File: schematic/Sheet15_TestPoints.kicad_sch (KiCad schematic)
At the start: 18 parts

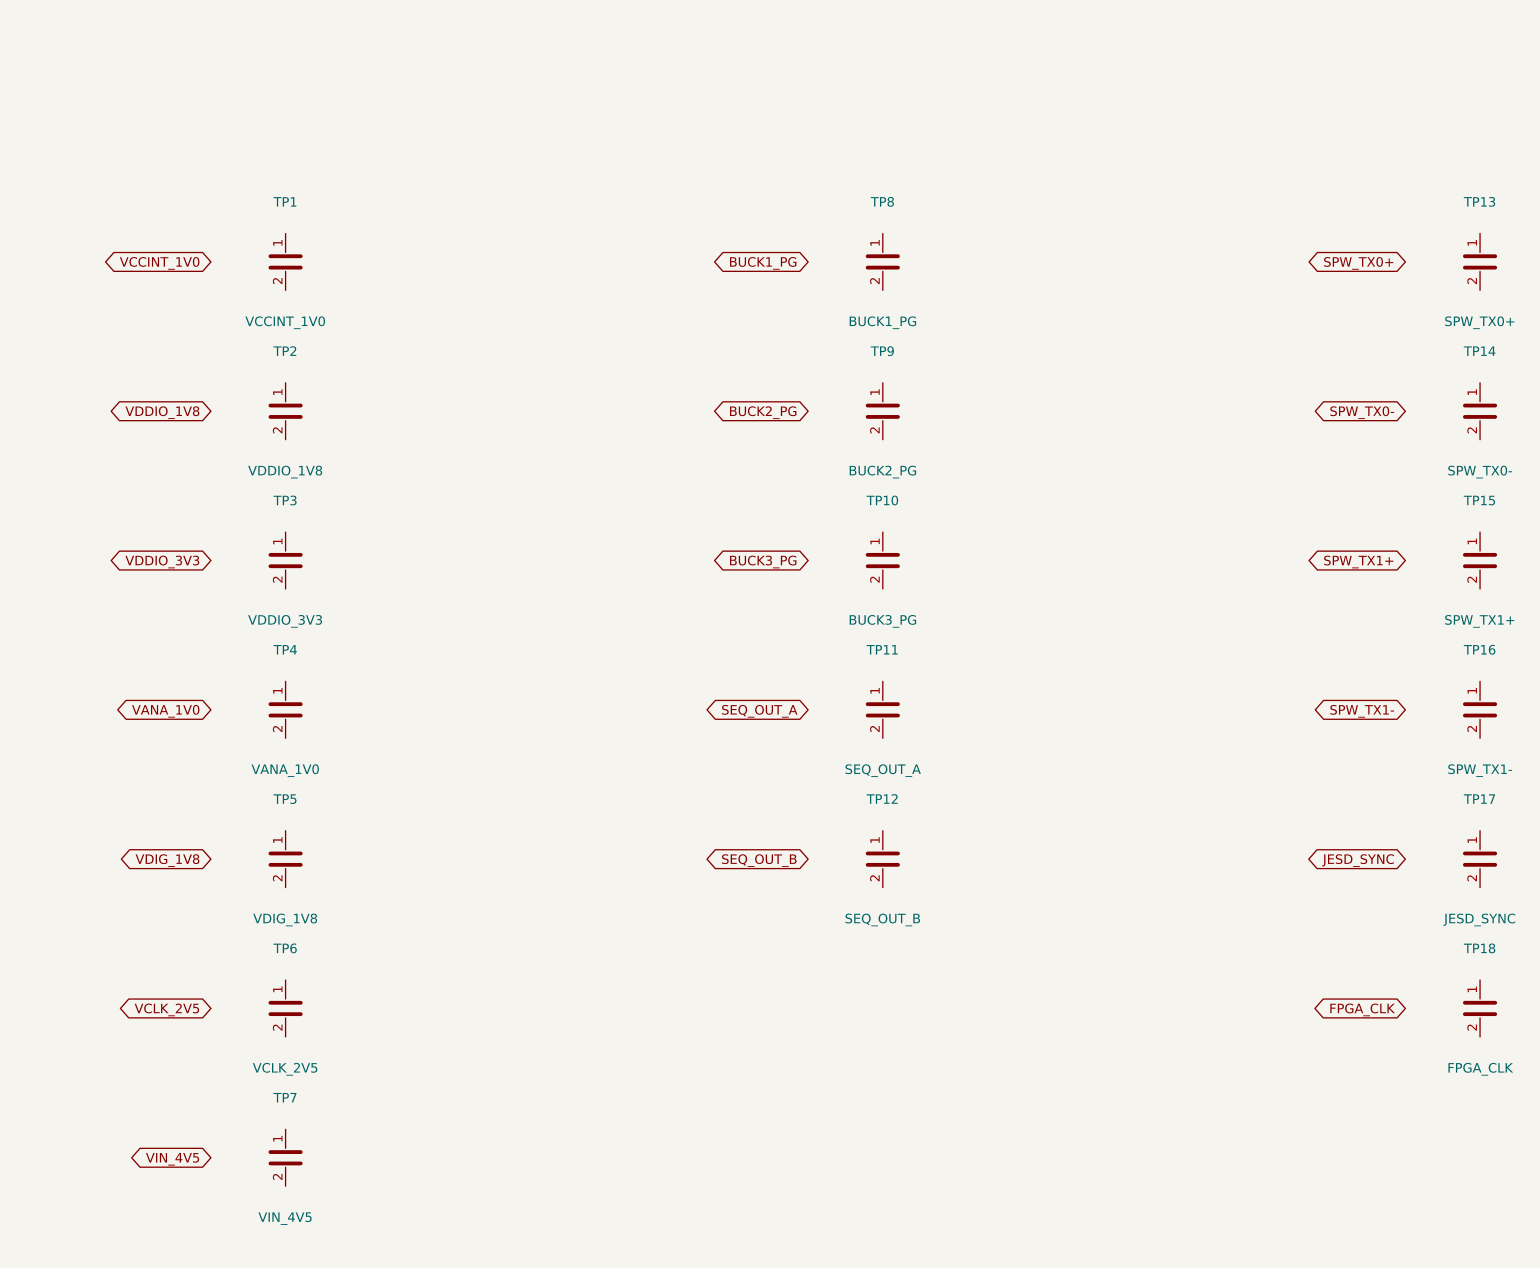
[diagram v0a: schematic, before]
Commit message: feat: real IC schematics with proper pin connections
- ADC12DJ5200-SP: 20 left pins (power, SPI, analog) + 21 right pins (JESD204C)
- XQRVC1902-SP: 19 left pins (power) + 30 right pins (JTAG, SPW, JESD, config)
- TPS7H5002-SP: 9 left + 7 right pins (buck converter 1.0V core)
- ISL70003ASEH: 7 left + 5 right (buck 1.8V/3.3V)
- LMX2615-SP: 8+8 pins (PLL synthesizer)
- LMK04832-SP: 12+12 pins (clock distributor)
- TPS7H1111-SP / TPS7H1121-SP: 3+3 pins (LDOs)
- TPS7H3014-SP: 4+4 pins (sequencer)
- INA214-SP: 3+2 pins (current sense)
- CVHD-950: 3+2 pins (VCXO)

Sheets:
- 02: SMA→50Ω match→anti-alias→ADC analog input
- 03: ADC decoupling, JESD outputs, SPI control
- 04: FPGA 14x decoupling caps, JTAG, SPW, JESD
- 05: Crystek→LMX2615→LMK04832→ADC+FPGA clock tree
- 06-09: Power input, TPS7H5002 buck 1.0V, ISL70003A buck 1.8V/3.3V
- 10-12: LDO 1.0V analog, 1.8V digital, 2.5V clock
- 13: 2x TPS7H3014 power sequencer
- 14: JTAG/SPW/UART connectors
- 15-17: Test points, decoupling, power tree diagram

All 17 sheets export via kicad-cli, merged PDF: 1.1MB
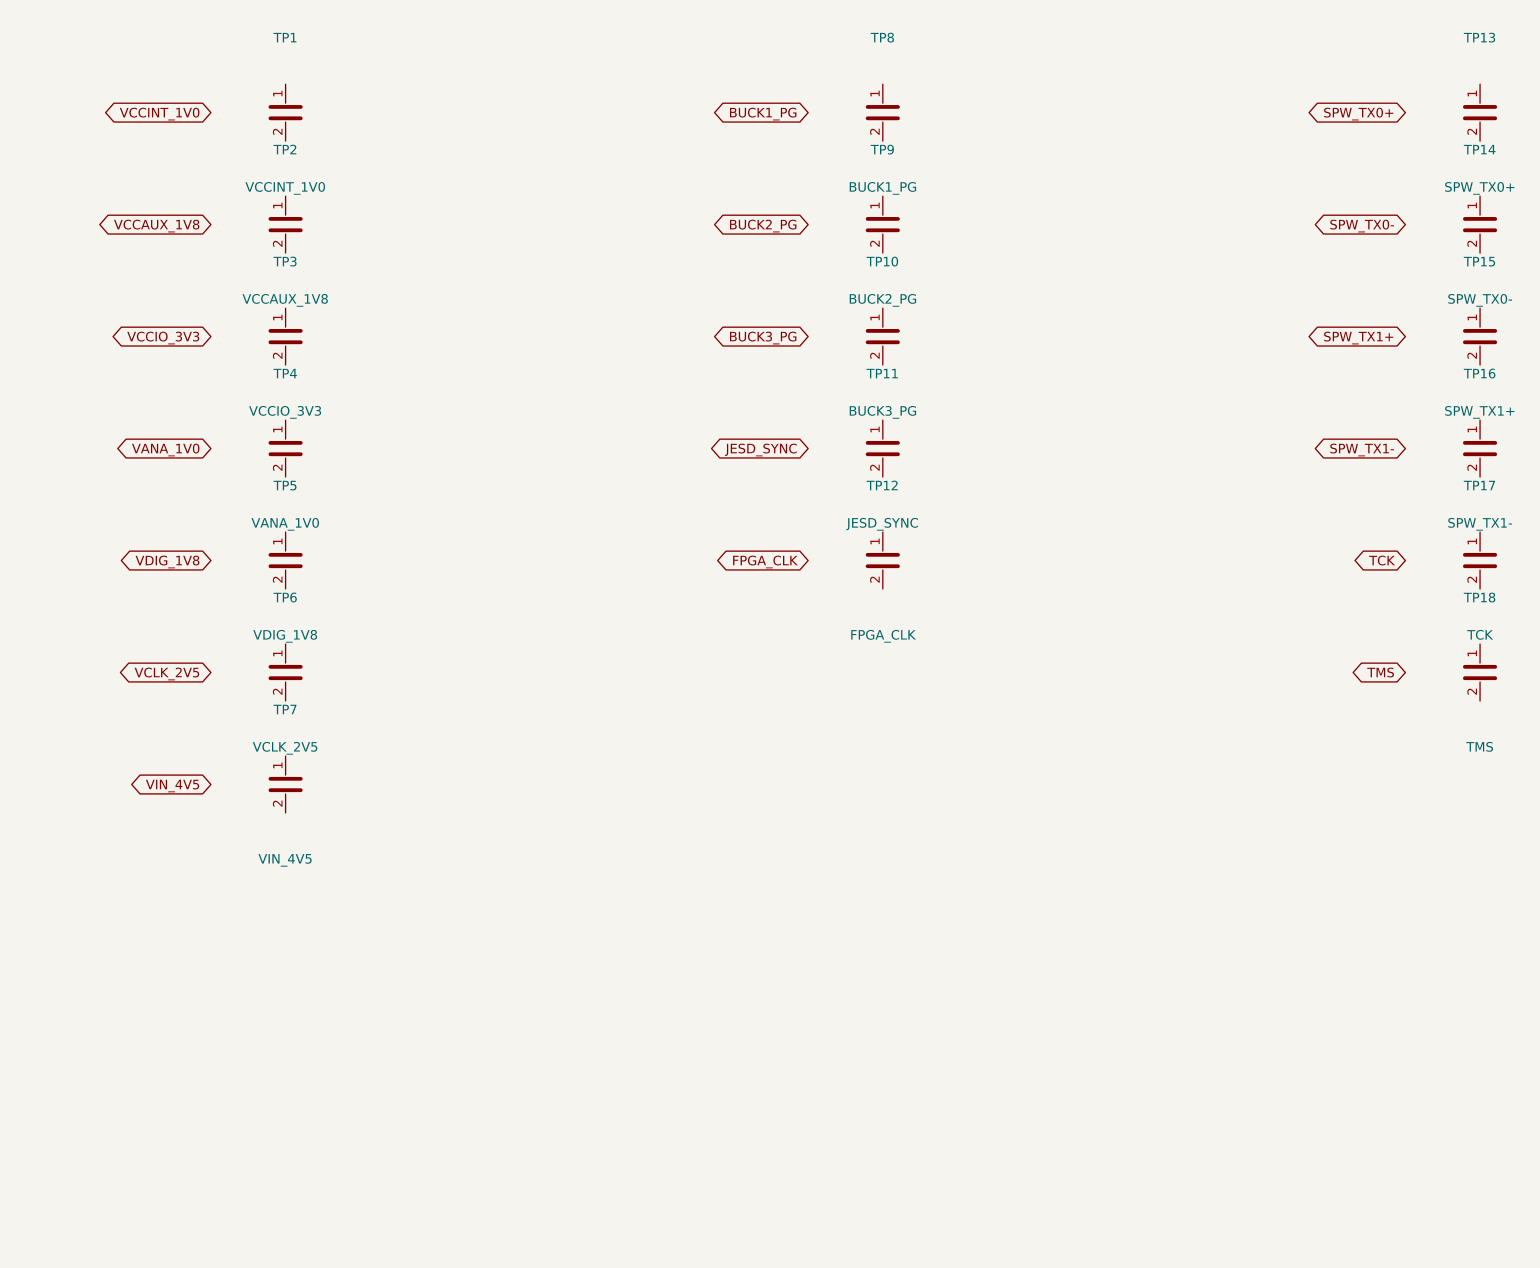
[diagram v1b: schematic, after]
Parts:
- TP1, TP10, TP13, TP14, TP15, TP16, TP4, TP5, TP6, TP7, TP8, TP9: footprint TestPoint:TestPoint_Pad_1.5x1.5mm -> TestPoint
- TP11: value SEQ_OUT_A -> JESD_SYNC; footprint TestPoint:TestPoint_Pad_1.5x1.5mm -> TestPoint
- TP12: value SEQ_OUT_B -> FPGA_CLK; footprint TestPoint:TestPoint_Pad_1.5x1.5mm -> TestPoint
- TP17: value JESD_SYNC -> TCK; footprint TestPoint:TestPoint_Pad_1.5x1.5mm -> TestPoint
- TP18: value FPGA_CLK -> TMS; footprint TestPoint:TestPoint_Pad_1.5x1.5mm -> TestPoint
- TP2: value VDDIO_1V8 -> VCCAUX_1V8; footprint TestPoint:TestPoint_Pad_1.5x1.5mm -> TestPoint
- TP3: value VDDIO_3V3 -> VCCIO_3V3; footprint TestPoint:TestPoint_Pad_1.5x1.5mm -> TestPoint

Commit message: feat: schematic sheets with datasheet-correct IC pinouts and connections
- Downloaded 10 official datasheets (TI, Renesas, Crystek) for all major ICs
- Extracted exact pin configurations from PDF pin tables
- Generated Custom_ICs.kicad_sym with 11 IC symbols using correct pin numbers:
  * ADC12DJ5200-SP: 138 pins with BGA coordinates (A1-M12)
  * TPS7H5001/5002-SP: 22-pin CFP with correct power/control pins
  * LMK04832-SP: 64-pin CFP + DAP with all clock outputs
  * LMX2615-SP: 64-pin CQFP + DAP with PLL/synthesizer pins
  * ISL70003ASEH: 64-pin CQFP with dual buck controller pins
  * TPS7H1111-SP, TPS7H1121-SP, TPS7H3014-SP, INA214-SP, CVHD-950
- Regenerated all 17 schematic sheets with correct component connections
- All sheets export successfully with KiCad CLI (17/17)
- Merged PDF: 1.3MB, 17 pages
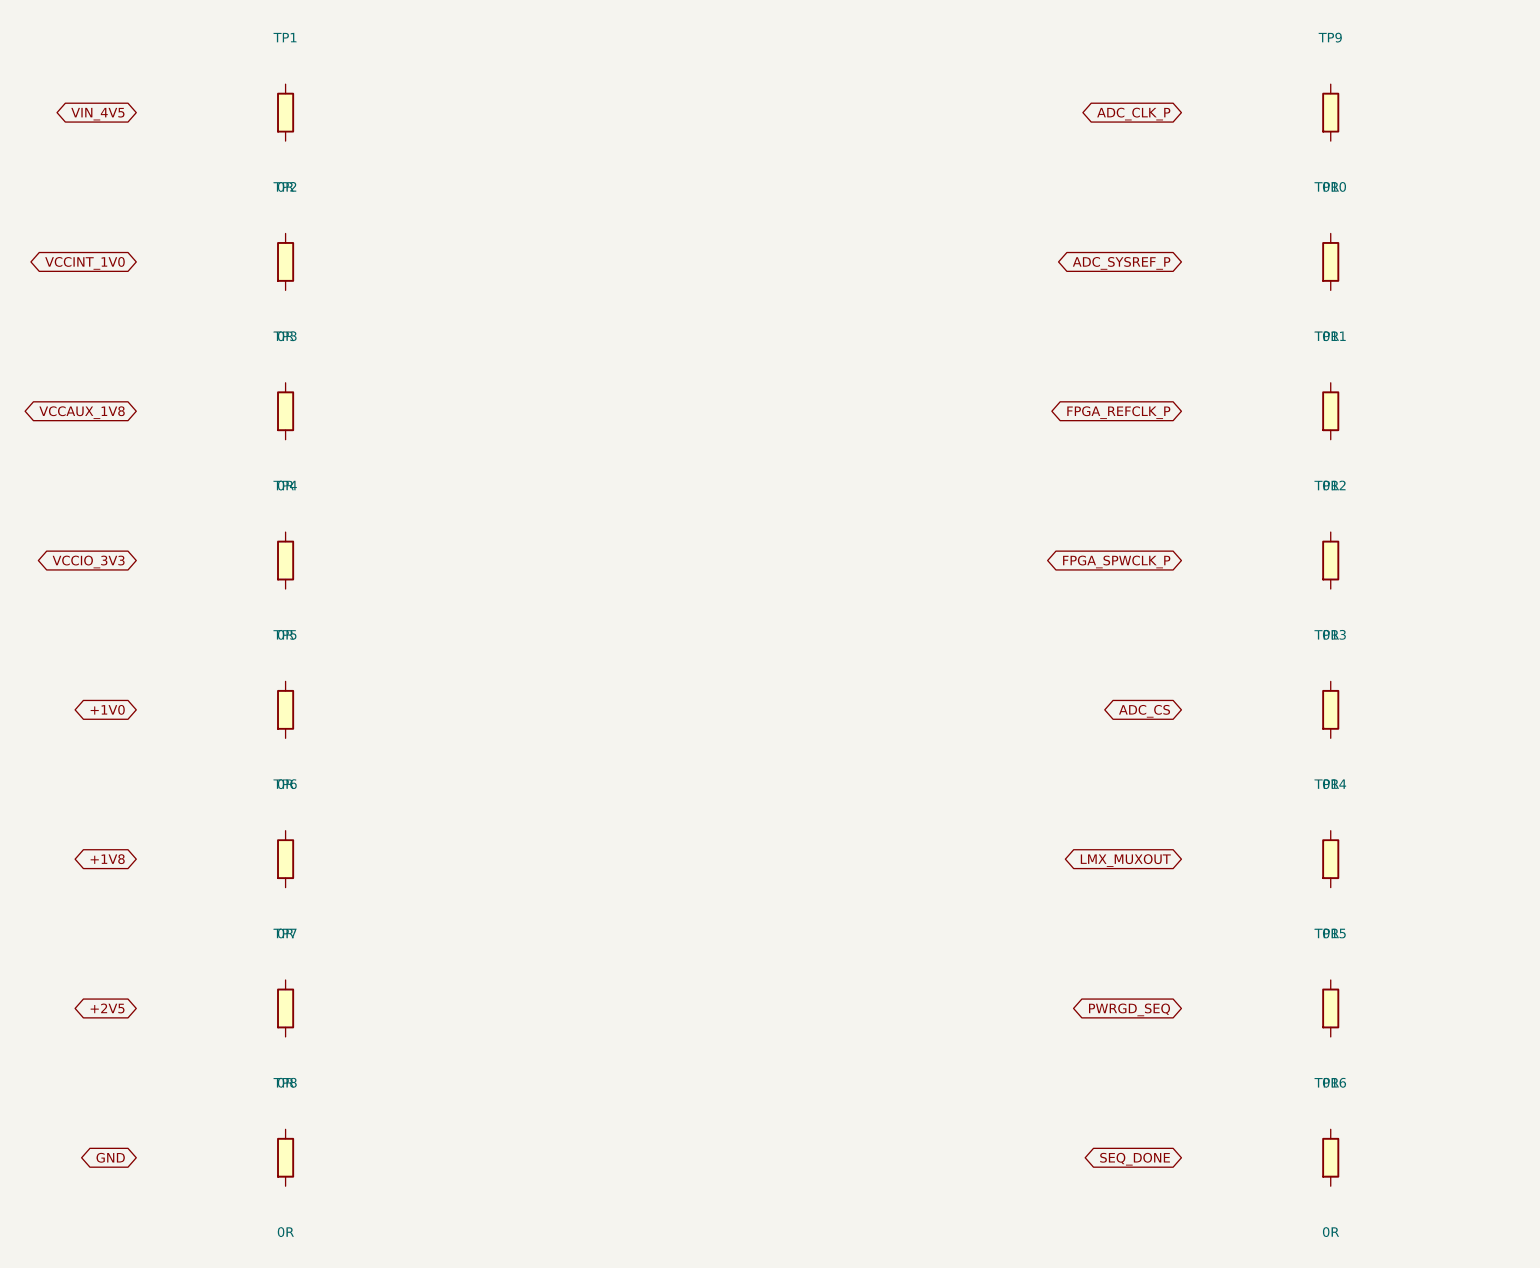
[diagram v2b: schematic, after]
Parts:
- removed TP1: VCCINT_1V0, TestPoint, symbol Device:C
- removed TP10: BUCK3_PG, TestPoint, symbol Device:C
- removed TP11: JESD_SYNC, TestPoint, symbol Device:C
- removed TP12: FPGA_CLK, TestPoint, symbol Device:C
- removed TP13: SPW_TX0+, TestPoint, symbol Device:C
- removed TP14: SPW_TX0-, TestPoint, symbol Device:C
- removed TP15: SPW_TX1+, TestPoint, symbol Device:C
- removed TP16: SPW_TX1-, TestPoint, symbol Device:C
- removed TP17: TCK, TestPoint, symbol Device:C
- removed TP18: TMS, TestPoint, symbol Device:C
- removed TP2: VCCAUX_1V8, TestPoint, symbol Device:C
- removed TP3: VCCIO_3V3, TestPoint, symbol Device:C
- removed TP4: VANA_1V0, TestPoint, symbol Device:C
- removed TP5: VDIG_1V8, TestPoint, symbol Device:C
- removed TP6: VCLK_2V5, TestPoint, symbol Device:C
- removed TP7: VIN_4V5, TestPoint, symbol Device:C
- removed TP8: BUCK1_PG, TestPoint, symbol Device:C
- removed TP9: BUCK2_PG, TestPoint, symbol Device:C
- added TP1, TP10, TP11, TP12, TP13, TP14, TP15, TP16, TP2, TP3, TP4, TP5, TP6, TP7, TP8, TP9: 0R, R_0402, symbol Device:R
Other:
- title: X-Band Digital Module 20x20cm -> X-Band Test Points
